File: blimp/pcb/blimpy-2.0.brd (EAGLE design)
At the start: 80 x 70 mm, 157 parts, among them J1 MICRO-USB, J10 3-PIN SMD, J11 3-PIN SMD, J12 3-PIN SMD, J13 3-PIN SMD, J14 3-PIN SMD, J15 3-PIN SMD, J9 3-PIN SMD, M0 DRV8833PWPR, M1 DRV8833PWPR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

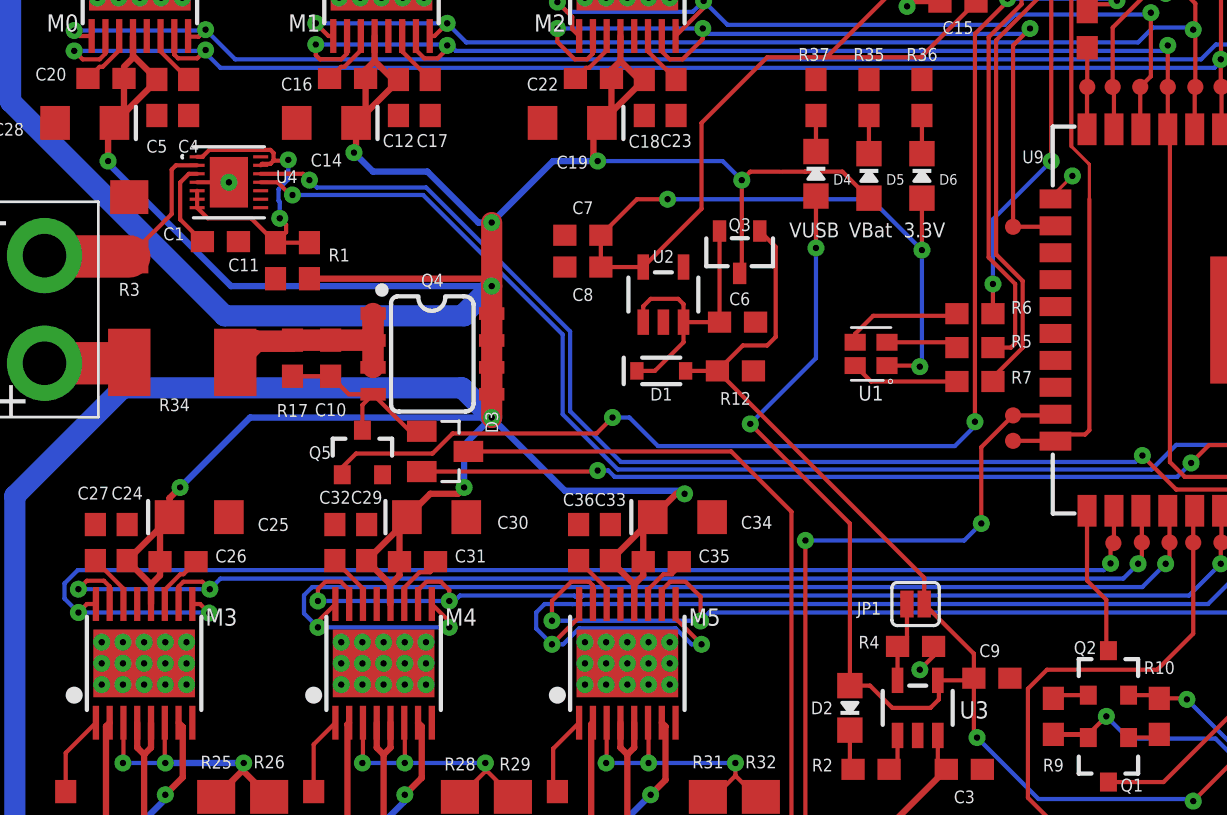
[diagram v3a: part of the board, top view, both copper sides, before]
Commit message: Added jumper to disable charging when MC is running
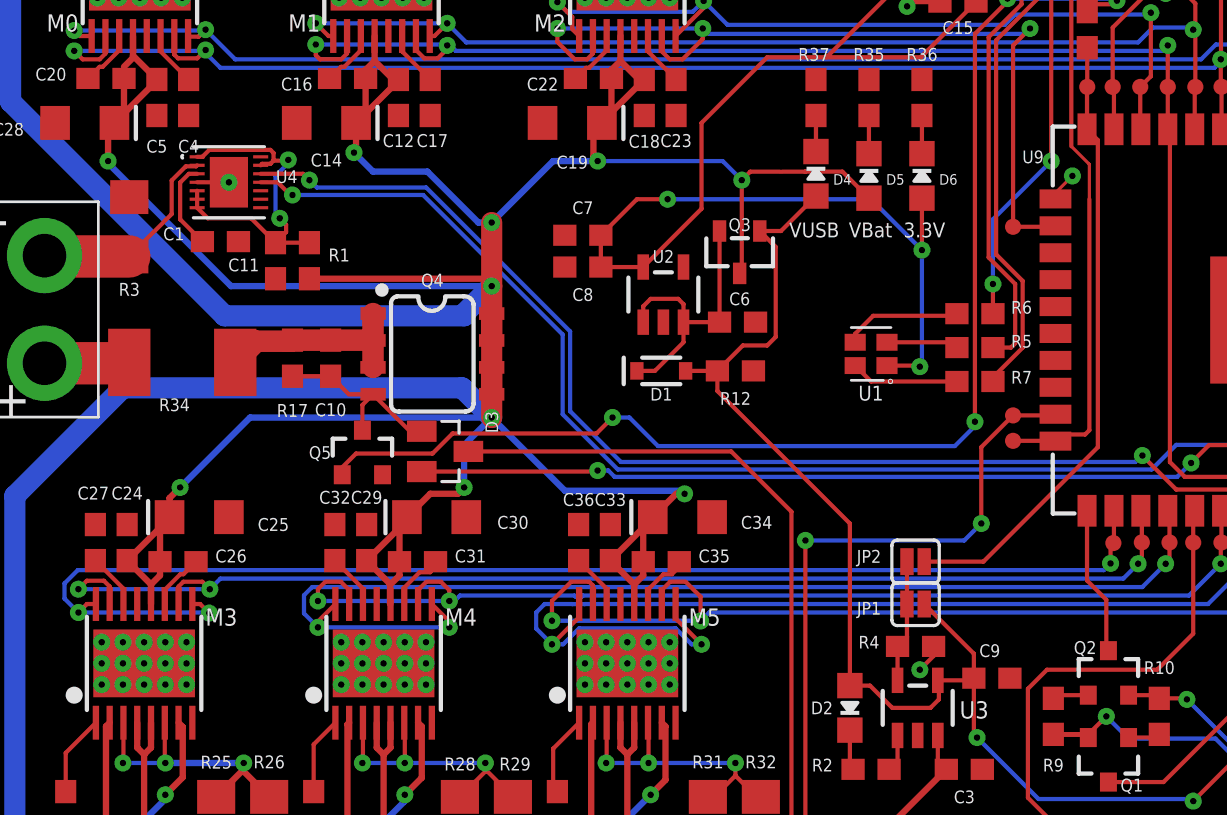
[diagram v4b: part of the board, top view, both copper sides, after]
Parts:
- added JP2: JUMPER-SMT_2_NO_SILK, SparkFun-Jumpers:SMT-JUMPER_2_NO_SILK
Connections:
- net N$4: now also JP2.1
- net PWR: now also JP2.2
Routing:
- net PWR: track 3.85 -> 29.5 mm
- net V_USB: track 99.6 -> 79.0 mm, vias 6 -> 4
- net N$4: track 3.78 -> 5.78 mm
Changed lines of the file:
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@@
 <attribute name="PROD_ID" value="RES-07868" x="62.4" y="48.3" size="1.778" layer="27" rot="R90" display="off"/>
+</element>
+<element name="JP2" library="SparkFun-Jumpers" library_urn="urn:adsk.eagle:library:528" package="SMT-JUMPER_2_NO_SILK" package3d_urn="urn:adsk.eagle:package:39279/1" value="JUMPER-SMT_2_NO_SILK" x="44.1" y="23.6" smashed="yes">
+<attribute name="NAME" x="41.9" y="23.543" size="0.6096" layer="25" font="vector" ratio="20" align="bottom-center"/>
 </element>
 </elements>
@@
 <wire x1="43.6936" y1="20.0436" x2="43.25" y2="19.6" width="0.2" layer="1"/>
 <wire x1="43.25" y1="19.6" x2="43.25" y2="18.0001" width="0.2" layer="1"/>
+<contactref element="JP2" pad="1"/>
+<wire x1="43.6936" y1="21.6" x2="43.6936" y2="23.6" width="0.2" layer="1"/>
 </signal>
 <signal name="3.3V">
@@
 <wire x1="57.2" y1="12.3" x2="59.08469375" y2="14.18469375" width="0.2" layer="1"/>
 <wire x1="59.08469375" y1="14.18469375" x2="60.7436" y2="14.18469375" width="0.2" layer="1"/>
-<wire x1="34.75" y1="32.6" x2="44.5064" y2="22.8436" width="0.2" layer="1"/>
-<wire x1="44.5064" y1="22.8436" x2="44.5064" y2="21.6" width="0.2" layer="1"/>
-<via x="36.3" y="30.1" extent="1-16" drill="0.3"/>
-<via x="39.4" y="38.4" extent="1-16" drill="0.3"/>
-<wire x1="39.4" y1="33.2" x2="39.4" y2="38.4" width="0.2" layer="16"/>
-<wire x1="36.3" y1="30.1" x2="39.4" y2="33.2" width="0.2" layer="16"/>
 <wire x1="75.55" y1="15.6436" x2="75.55" y2="16.4" width="0.2" layer="1"/>
 <wire x1="60.7436" y1="14.18469375" x2="74.09109375" y2="14.18469375" width="0.2" layer="16"/>
@@
 <wire x1="46.85" y1="19.2564" x2="44.5064" y2="21.6" width="0.2" layer="1"/>
 <contactref element="D4" pad="A"/>
-<wire x1="39.4" y1="38.4" x2="39.4" y2="40.85" width="0.2" layer="1"/>
-<wire x1="36.3" y1="30.1" x2="41" y2="25.4" width="0.2" layer="1"/>
-<wire x1="41" y1="25.4" x2="41" y2="17.75" width="0.2" layer="1"/>
+<wire x1="41" y1="25.3" x2="41" y2="17.75" width="0.2" layer="1"/>
+<wire x1="36.75" y1="39.2" x2="37.75" y2="39.2" width="0.2" layer="1"/>
+<wire x1="37.75" y1="39.2" x2="39.4" y2="40.85" width="0.2" layer="1"/>
+<wire x1="34.75" y1="32.6" x2="34.75" y2="31.65" width="0.2" layer="1"/>
+<wire x1="41" y1="25.4" x2="41" y2="25.3" width="0.2" layer="1"/>
+<wire x1="34.75" y1="31.65" x2="41" y2="25.4" width="0.2" layer="1"/>
 </signal>
 <signal name="V_BATT">
@@
 <via x="14.5" y="42.5564" extent="1-16" drill="0.3"/>
 <via x="14.1" y="39.8" extent="1-16" drill="0.3"/>
-<wire x1="14.0436" y1="41.17189375" x2="14.0436" y2="40.62810625" width="0.2" layer="16"/>
-<wire x1="14.5" y1="42.5564" x2="14.5" y2="41.62829375" width="0.2" layer="16"/>
-<wire x1="14.5" y1="41.62829375" x2="14.0436" y2="41.17189375" width="0.2" layer="16"/>
-<wire x1="14.0436" y1="40.62810625" x2="14.1" y2="40.57170625" width="0.2" layer="16"/>
-<wire x1="14.1" y1="40.57170625" x2="14.1" y2="39.8" width="0.2" layer="16"/>
 <wire x1="14.1" y1="39.8" x2="14.4" y2="39.5" width="0.2" layer="1"/>
 <wire x1="14.4" y1="39.5" x2="14.4" y2="39.15" width="0.2" layer="1"/>
+<wire x1="14.5" y1="42.5564" x2="14.5" y2="42.4" width="0.2" layer="16"/>
+<wire x1="14.5" y1="42.4" x2="13.9" y2="41.8" width="0.2" layer="16"/>
+<wire x1="13.9" y1="41.8" x2="13.9" y2="40" width="0.2" layer="16"/>
+<wire x1="13.9" y1="40" x2="14.1" y2="39.8" width="0.2" layer="16"/>
 </signal>
 <signal name="N$14">
@@
 <wire x1="52.2" y1="47.85" x2="52.2" y2="46" width="0.2" layer="1"/>
 <wire x1="52.2" y1="46" x2="52.19" y2="45.99" width="0.2" layer="1"/>
+<contactref element="JP2" pad="2"/>
+<wire x1="44.5064" y1="23.6" x2="47.3" y2="23.6" width="0.2" layer="1"/>
+<wire x1="47.3" y1="23.6" x2="52.7" y2="29" width="0.2" layer="1"/>
+<wire x1="52.7" y1="29" x2="52.7" y2="43.49" width="0.2" layer="1"/>
+<wire x1="52.7" y1="43.49" x2="52.19" y2="44" width="0.2" layer="1"/>
 </signal>
 <signal name="BTN">
@@
 <contactref element="R3" pad="2"/>
 <contactref element="J2" pad="2"/>
-<wire x1="7" y1="38" x2="9" y2="40" width="0.2" layer="1"/>
-<wire x1="9" y1="40" x2="9" y2="42.1" width="0.2" layer="1"/>
-<wire x1="9" y1="42.1" x2="9.2" y2="42.3" width="0.2" layer="1"/>
-<wire x1="9.2" y1="42.3" x2="10.2014" y2="42.3" width="0.2" layer="1"/>
+<wire x1="9" y1="40" x2="7" y2="38" width="0.2" layer="1"/>
 <wire x1="7" y1="38" x2="3.04" y2="38" width="2" layer="1"/>
 <wire x1="3.04" y1="38" x2="3" y2="38.04" width="2" layer="1"/>
+<wire x1="10.2014" y1="42.3" x2="10.1538" y2="42.2524" width="0.2" layer="1"/>
+<wire x1="10.1538" y1="42.2524" x2="9.666675" y2="42.2524" width="0.2" layer="1"/>
+<wire x1="9.666675" y1="42.2524" x2="9" y2="41.585725" width="0.2" layer="1"/>
+<wire x1="9" y1="41.585725" x2="9" y2="40" width="0.2" layer="1"/>
 </signal>
 <signal name="N$18">
